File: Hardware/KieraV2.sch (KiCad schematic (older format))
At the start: 42 parts, among them J1 Conn_01x05_Male, J2 Conn_01x04_Male, SW1 SW_Rotary2x4, SW2 SW_Rotary2x4, SW3 SW_Push, SW4 SW_Push, SW5 SW_Push, SW6 SW_MEC_5G, U1 STM32L4P5RET6, Y1 8MHz

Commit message: added footprints, updated CAN, annotated symbols
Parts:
- C1: renamed from C14; footprint (none) -> Capacitor_SMD:C_0603_1608Metric
- C10: renamed from C9; footprint (none) -> Capacitor_SMD:C_0603_1608Metric
- C11: renamed from C17; footprint (none) -> Capacitor_SMD:C_0603_1608Metric
- C12: renamed from C11; footprint (none) -> Capacitor_SMD:C_0603_1608Metric
- C13: renamed from C12; footprint (none) -> Capacitor_SMD:C_0603_1608Metric
- C14: renamed from C13; footprint (none) -> Capacitor_SMD:C_0603_1608Metric
- C15: renamed from C10; footprint (none) -> Capacitor_SMD:C_0603_1608Metric
- C2: renamed from C15; footprint (none) -> Capacitor_SMD:C_0603_1608Metric
- C3: renamed from C18; footprint (none) -> Capacitor_SMD:C_0603_1608Metric
- C4: renamed from C16; footprint (none) -> Capacitor_SMD:C_0603_1608Metric
- C5: renamed from C19; footprint (none) -> Capacitor_SMD:C_0603_1608Metric
- C6: renamed from C20; footprint (none) -> Capacitor_SMD:C_0603_1608Metric
- C7: renamed from C6; footprint (none) -> Capacitor_SMD:C_0603_1608Metric
- C8: renamed from C7; footprint (none) -> Capacitor_SMD:C_0603_1608Metric
- C9: renamed from C8; footprint (none) -> Capacitor_SMD:C_0603_1608Metric
- R1, R2, R3, R6, R7, R8: footprint (none) -> Resistor_SMD:R_0603_1608Metric
- R10: renamed from R9; footprint (none) -> Resistor_SMD:R_0603_1608Metric
- R11: renamed from R16; footprint (none) -> Resistor_SMD:R_0603_1608Metric
- R12: renamed from R17; footprint (none) -> Resistor_SMD:R_0603_1608Metric
- R13: renamed from R11; footprint (none) -> Resistor_SMD:R_0603_1608Metric
- R14: renamed from R18; footprint (none) -> Resistor_SMD:R_0603_1608Metric
- R15: renamed from R12; footprint (none) -> Resistor_SMD:R_0603_1608Metric
- R16: renamed from R19; footprint (none) -> Resistor_SMD:R_0603_1608Metric
- R17: renamed from R13; footprint (none) -> Resistor_SMD:R_0603_1608Metric
- R4: renamed from R5; footprint (none) -> Resistor_SMD:R_0603_1608Metric
- R5: renamed from R4; footprint (none) -> Resistor_SMD:R_0603_1608Metric
- R9: renamed from R10; footprint (none) -> Resistor_SMD:R_0603_1608Metric
- SW1, SW2: footprint (none) -> Rotary_Encoder:SW_Rotary2x4
- SW4: renamed from SW6; footprint (none) -> Button_Switch_SMD:SW_Push_1P1T_NO_6x6mm_H9.5mm
- Y1: footprint (none) -> Crystal:Crystal_SMD_HC49-SD
- renumbered J2 to J1, J1 to J2, SW4 to SW5, SW5 to SW6
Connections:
- net labels added: CANH, CANL
- no-connect marks 0 -> 44

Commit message: added temp pushbutton footprint
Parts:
- SW3, SW5, SW6: footprint (none) -> Button_Switch_THT:MyPushbuttonSwitch
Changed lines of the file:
@@
 F 0 "SW3" H 1450 3485 50  0000 C CNN
 F 1 "SW_Push" H 1450 3394 50  0000 C CNN
-F 2 "" H 1450 3400 50  0001 C CNN
+F 2 "Button_Switch_THT:MyPushbuttonSwitch" H 1450 3400 50  0001 C CNN
 F 3 "~" H 1450 3400 50  0001 C CNN
 	1    1450 3200
@@
 F 0 "SW5" H 1450 4085 50  0000 C CNN
 F 1 "SW_Push" H 1450 3994 50  0000 C CNN
-F 2 "" H 1450 4000 50  0001 C CNN
+F 2 "Button_Switch_THT:MyPushbuttonSwitch" H 1450 4000 50  0001 C CNN
 F 3 "~" H 1450 4000 50  0001 C CNN
 	1    1450 3800
@@
 F 0 "SW6" H 1450 4685 50  0000 C CNN
 F 1 "SW_Push" H 1450 4594 50  0000 C CNN
-F 2 "" H 1450 4600 50  0001 C CNN
+F 2 "Button_Switch_THT:MyPushbuttonSwitch" H 1450 4600 50  0001 C CNN
 F 3 "~" H 1450 4600 50  0001 C CNN
 	1    1450 4400

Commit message: small changes to footprints
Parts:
- J1: footprint (none) -> Connector_PinHeader_1.00mm:PinHeader_1x04_P1.00mm_Vertical
- J2: footprint (none) -> Connector_PinHeader_1.00mm:PinHeader_1x05_P1.00mm_Vertical
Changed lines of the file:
@@
 F 0 "J1" H 10000 950 50  0000 R CNN
 F 1 "Conn_01x04_Male" H 10000 850 50  0000 R CNN
-F 2 "" H 10050 950 50  0001 C CNN
+F 2 "Connector_PinHeader_1.00mm:PinHeader_1x04_P1.00mm_Vertical" H 10050 950 50  0001 C CNN
 F 3 "~" H 10050 950 50  0001 C CNN
 	1    10050 950
@@
 F 0 "J2" H 7950 1150 50  0000 C CNN
 F 1 "Conn_01x05_Male" H 7650 1050 50  0000 C CNN
-F 2 "" H 8050 1100 50  0001 C CNN
+F 2 "Connector_PinHeader_1.00mm:PinHeader_1x05_P1.00mm_Vertical" H 8050 1100 50  0001 C CNN
 F 3 "~" H 8050 1100 50  0001 C CNN
 	1    8050 1100

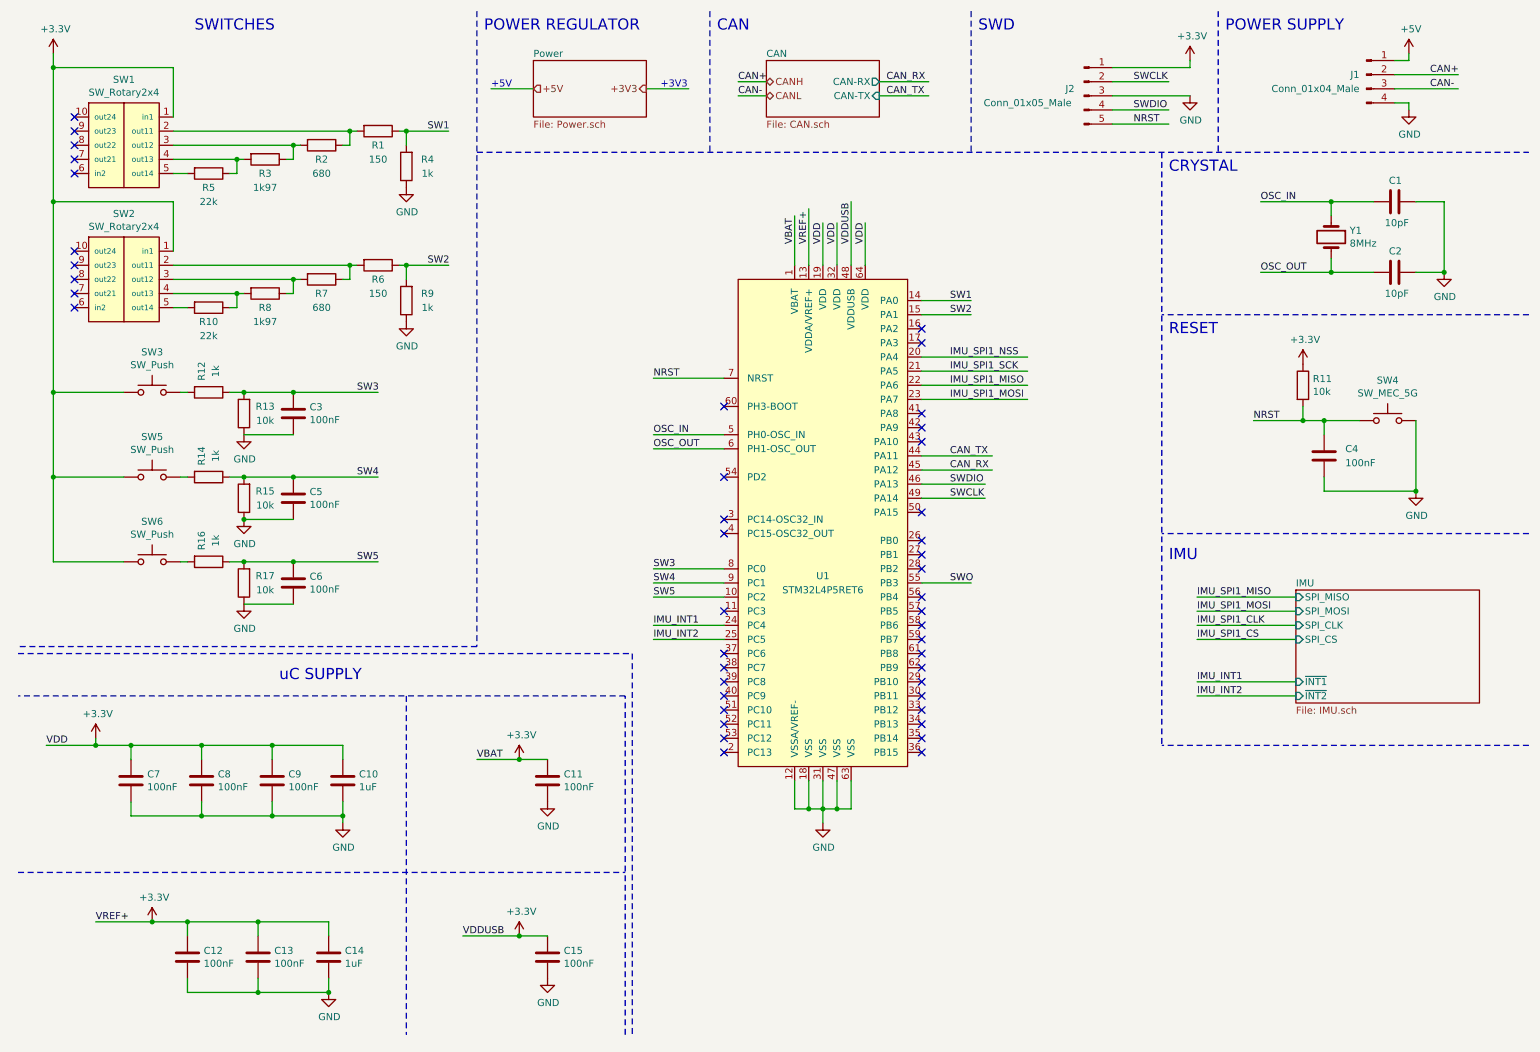
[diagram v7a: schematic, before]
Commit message: small changes to the electrical schematic, added footprints, first go at designing the pcb
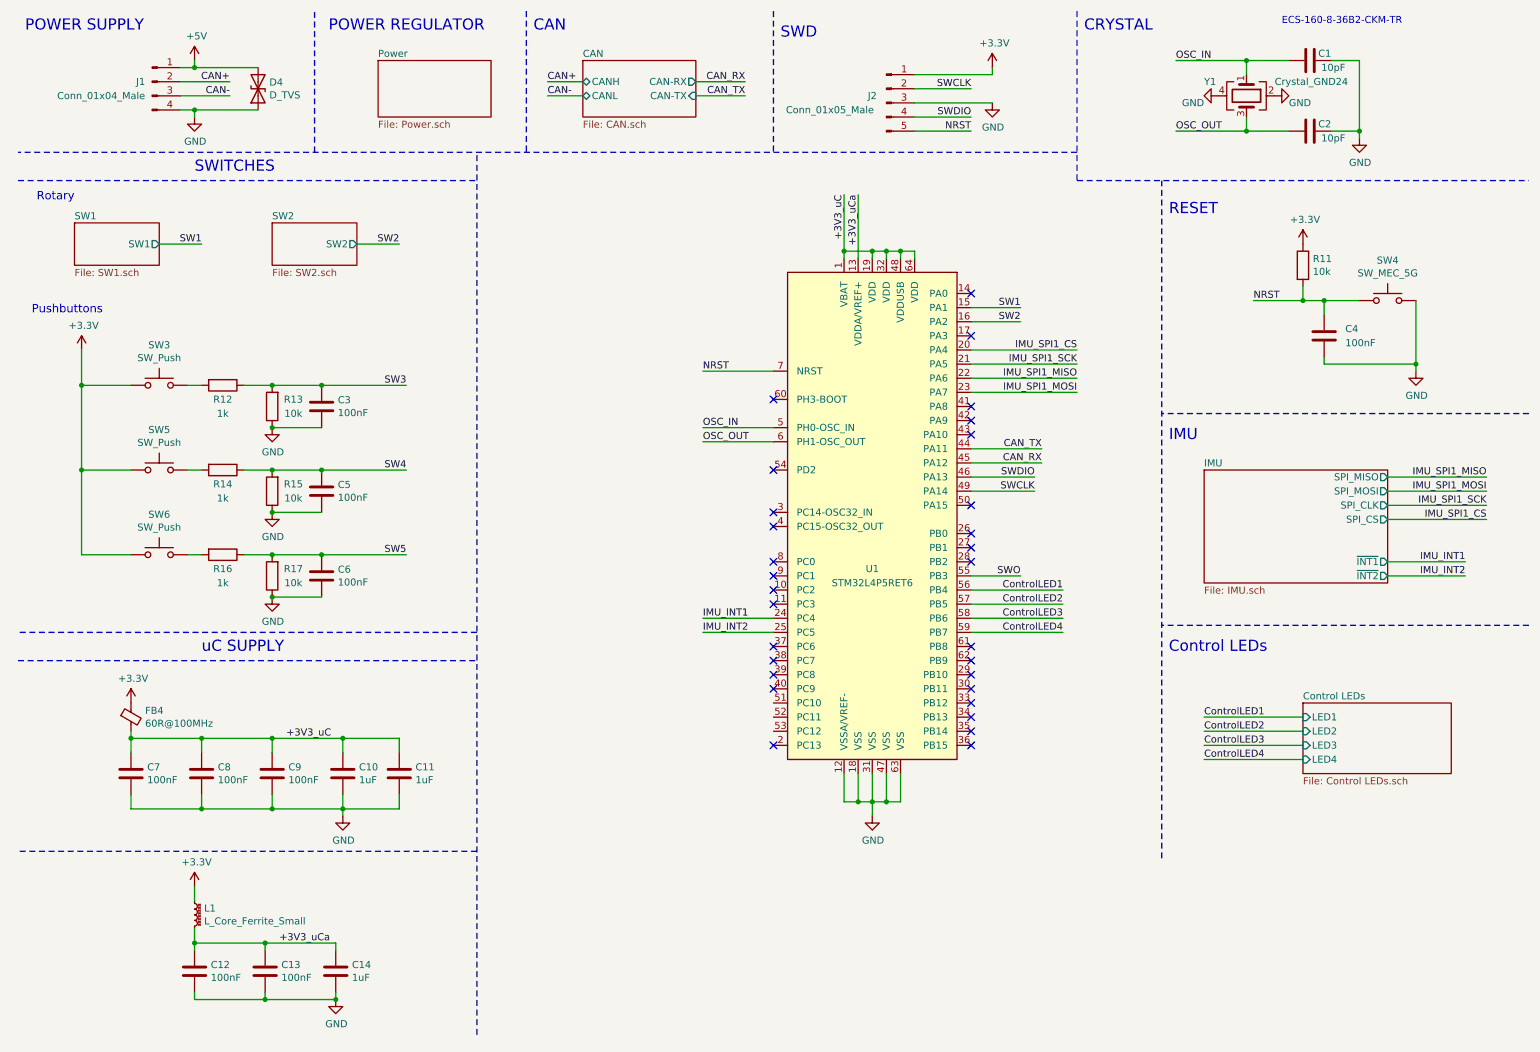
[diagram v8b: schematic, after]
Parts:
- removed C15: 100nF, Capacitor_SMD:C_0603_1608Metric, symbol Device:C
- removed R1, R6: 150, Resistor_SMD:R_0603_1608Metric, symbol Device:R
- removed R10, R5: 22k, Resistor_SMD:R_0603_1608Metric, symbol Device:R
- removed R2, R7: 680, Resistor_SMD:R_0603_1608Metric, symbol Device:R
- removed R3, R8: 1k97, Resistor_SMD:R_0603_1608Metric, symbol Device:R
- removed R4, R9: 1k, Resistor_SMD:R_0603_1608Metric, symbol Device:R
- removed SW1, SW2: SW_Rotary2x4, Rotary_Encoder:SW_Rotary2x4, symbol Switch:SW_Rotary2x4
- removed Y1: 8MHz, Crystal:Crystal_SMD_HC49-SD, symbol Device:Crystal
- added D4: D_TVS, Diode_SMD:D_1210_3225Metric, symbol Device:D_TVS
- added FB4: 60R@100MHz, Inductor_SMD:L_0603_1608Metric, symbol Device:Ferrite_Bead_Small
- added L1: L_Core_Ferrite_Small, Inductor_SMD:L_0805_2012Metric, symbol Device:L_Core_Ferrite_Small
- added Y1: Crystal_GND24, Crystal:Crystal_SMD_2520-4Pin_2.5x2.0mm, symbol Device:Crystal_GND24
- C11: value 100nF -> 1uF
- J1: footprint Connector_PinHeader_1.00mm:PinHeader_1x04_P1.00mm_Vertical -> Connector_PinHeader_2.54mm:PinHeader_1x04_P2.54mm_Vertical
- J2: footprint Connector_PinHeader_1.00mm:PinHeader_1x05_P1.00mm_Vertical -> Connector_PinHeader_2.54mm:PinHeader_1x05_P2.54mm_Vertical
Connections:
- net labels added: +3V3_uC, +3V3_uCa, ControlLED1, ControlLED2, ControlLED3, ControlLED4
- net labels removed: +3V3, CANH, CANL, IMU_SPI1_CLK, IMU_SPI1_NSS, VBAT, VDD, VDDUSB, VREF+
- wire segments 169 -> 143
- no-connect marks 44 -> 30
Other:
- note added: "Control LEDs"
- note added: "ECS-160-8-36B2-CKM-TR"
- note added: "Pushbuttons"
- note added: "Rotary\n"
- note removed: "+3V3"
- note removed: "+5V\n"
- moved on the sheet: C1, C10, C12, C13, C14, C2, C3, C4, C5, C6, C7, C8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
